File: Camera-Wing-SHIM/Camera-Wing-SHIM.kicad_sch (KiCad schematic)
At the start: 3 parts, among them J1 Pico RHS Headers, J2 Conn_01x06_Pin, J3 Conn_01x06_Socket

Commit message: Made PCB
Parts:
- J1: footprint (none) -> Footprints-General:Pico-Wing-Shim-SPI
- J2: value Conn_01x06_Pin -> Pin Connection
- J3: value Conn_01x06_Socket -> JST Connection; footprint Connector_JST:JST_XH_B7B-XH-A_1x07_P2.50mm_Vertical -> Connector_JST:JST_XH_B6B-XH-A_1x06_P2.50mm_Vertical
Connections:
- net +3V3: now also J2.1 (Pin_1), J3.1 (Pin_1)
- net CLK: now also J2.3 (Pin_3), J3.3 (Pin_3)
- net CS: now also J2.6 (Pin_6), J3.6 (Pin_6)
- net GND: now also J2.2 (Pin_2), J3.2 (Pin_2)
- net MISO: now also J2.4 (Pin_4), J3.4 (Pin_4)
- net MOSI: now also J2.5 (Pin_5), J3.5 (Pin_5)
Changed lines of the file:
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@@
+    (stroke (width 0) (type default))
+  )
+  (wire (pts (xy 133.35 78.74) (xy 139.7 78.74))
+    (stroke (width 0) (type default))
+  )
+  (wire (pts (xy 191.77 71.12) (xy 191.77 73.66))
     (stroke (width 0) (type default))
   )
@@
     (stroke (width 0) (type default))
   )
+  (wire (pts (xy 133.35 73.66) (xy 139.7 73.66))
+    (stroke (width 0) (type default))
+  )
+  (wire (pts (xy 147.32 68.58) (xy 147.32 66.04))
+    (stroke (width 0) (type default))
+  )
+  (wire (pts (xy 133.35 71.12) (xy 147.32 71.12))
+    (stroke (width 0) (type default))
+  )
   (wire (pts (xy 80.01 59.69) (xy 80.01 62.23))
     (stroke (width 0) (type default))
@@
     (stroke (width 0) (type default))
   )
+  (wire (pts (xy 177.8 78.74) (xy 184.15 78.74))
+    (stroke (width 0) (type default))
+  )
+  (wire (pts (xy 177.8 81.28) (xy 184.15 81.28))
+    (stroke (width 0) (type default))
+  )
+  (wire (pts (xy 191.77 68.58) (xy 191.77 66.04))
+    (stroke (width 0) (type default))
+  )
   (wire (pts (xy 71.12 90.17) (xy 82.55 90.17))
     (stroke (width 0) (type default))
@@
     (stroke (width 0) (type default))
   )
+  (wire (pts (xy 147.32 71.12) (xy 147.32 73.66))
+    (stroke (width 0) (type default))
+  )
+  (wire (pts (xy 133.35 76.2) (xy 139.7 76.2))
+    (stroke (width 0) (type default))
+  )
+  (wire (pts (xy 177.8 76.2) (xy 184.15 76.2))
+    (stroke (width 0) (type default))
+  )
   (wire (pts (xy 71.12 97.79) (xy 82.55 97.79))
     (stroke (width 0) (type default))
@@
     (stroke (width 0) (type default))
   )
+  (wire (pts (xy 177.8 73.66) (xy 184.15 73.66))
+    (stroke (width 0) (type default))
+  )
+  (wire (pts (xy 177.8 68.58) (xy 191.77 68.58))
+    (stroke (width 0) (type default))
+  )
+  (wire (pts (xy 133.35 81.28) (xy 139.7 81.28))
+    (stroke (width 0) (type default))
+  )
+  (wire (pts (xy 177.8 71.12) (xy 191.77 71.12))
+    (stroke (width 0) (type default))
+  )
+  (wire (pts (xy 133.35 68.58) (xy 147.32 68.58))
+    (stroke (width 0) (type default))
+  )
+  (label "MOSI" (at 184.15 78.74 180) (fields_autoplaced)
+    (effects (font (size 1.27 1.27)) (justify right bottom))
+  )
+  (label "CLK" (at 139.7 73.66 180) (fields_autoplaced)
+    (effects (font (size 1.27 1.27)) (justify right bottom))
+  )
+  (label "CS" (at 184.15 81.28 180) (fields_autoplaced)
+    (effects (font (size 1.27 1.27)) (justify right bottom))
+  )
   (label "MISO" (at 82.55 97.79 180) (fields_autoplaced)
     (effects (font (size 1.27 1.27)) (justify right bottom))
   )
+  (label "MISO" (at 184.15 76.2 180) (fields_autoplaced)
+    (effects (font (size 1.27 1.27)) (justify right bottom))
+  )
   (label "CS" (at 82.55 95.25 180) (fields_autoplaced)
     (effects (font (size 1.27 1.27)) (justify right bottom))
   )
+  (label "MOSI" (at 139.7 78.74 180) (fields_autoplaced)
+    (effects (font (size 1.27 1.27)) (justify right bottom))
+  )
   (label "MOSI" (at 82.55 87.63 180) (fields_autoplaced)
     (effects (font (size 1.27 1.27)) (justify right bottom))
   )
   (label "CLK" (at 82.55 90.17 180) (fields_autoplaced)
+    (effects (font (size 1.27 1.27)) (justify right bottom))
+  )
+  (label "CLK" (at 184.15 73.66 180) (fields_autoplaced)
+    (effects (font (size 1.27 1.27)) (justify right bottom))
+  )
+  (label "CS" (at 139.7 81.28 180) (fields_autoplaced)
+    (effects (font (size 1.27 1.27)) (justify right bottom))
+  )
+  (label "MISO" (at 139.7 76.2 180) (fields_autoplaced)
     (effects (font (size 1.27 1.27)) (justify right bottom))
   )
@@
       (effects (font (size 1.27 1.27)))
     )
-    (property "Footprint" "" (at 66.04 72.39 0)
+    (property "Footprint" "Footprints-General:Pico-Wing-Shim-SPI" (at 66.04 72.39 0)
       (effects (font (size 1.27 1.27)) hide)
     )
@@
     )
   )
+  (symbol (lib_id "power:GND") (at 147.32 73.66 0) (unit 1)
+    (in_bom yes) (on_board yes) (dnp no) (fields_autoplaced)
+    (property "Reference" "#PWR05" (at 147.32 80.01 0)
+      (effects (font (size 1.27 1.27)) hide)
+    )
+    (property "Value" "GND" (at 147.32 78.74 0)
+      (effects (font (size 1.27 1.27)))
+    )
+    (property "Footprint" "" (at 147.32 73.66 0)
+      (effects (font (size 1.27 1.27)) hide)
+    )
+    (property "Datasheet" "" (at 147.32 73.66 0)
+      (effects (font (size 1.27 1.27)) hide)
+    )
+    (pin "1")
+    (instances
+      (project "Camera-Wing-SHIM"
+        (path "/573a4d9c-bd0f-4c16-a1f5-7ab3d68c8cde"
+          (reference "#PWR05") (unit 1)
+        )
+      )
+    )
+  )
   (symbol (lib_id "Connector:Conn_01x06_Pin") (at 128.27 73.66 0) (unit 1)
     (in_bom yes) (on_board yes) (dnp no) (fields_autoplaced)
@@
       (effects (font (size 1.27 1.27)))
     )
-    (property "Value" "Conn_01x06_Pin" (at 128.905 66.04 0)
+    (property "Value" "Pin Connection" (at 128.905 66.04 0)
       (effects (font (size 1.27 1.27)))
     )
@@
     )
   )
+  (symbol (lib_id "power:+3V3") (at 147.32 66.04 0) (unit 1)
+    (in_bom yes) (on_board yes) (dnp no) (fields_autoplaced)
+    (property "Reference" "#PWR04" (at 147.32 69.85 0)
+      (effects (font (size 1.27 1.27)) hide)
+    )
+    (property "Value" "+3V3" (at 147.32 60.96 0)
+      (effects (font (size 1.27 1.27)))
+    )
+    (property "Footprint" "" (at 147.32 66.04 0)
+      (effects (font (size 1.27 1.27)) hide)
+    )
+    (property "Datasheet" "" (at 147.32 66.04 0)
+      (effects (font (size 1.27 1.27)) hide)
+    )
+    (pin "1")
+    (instances
+      (project "Camera-Wing-SHIM"
+        (path "/573a4d9c-bd0f-4c16-a1f5-7ab3d68c8cde"
+          (reference "#PWR04") (unit 1)
+        )
+      )
+    )
+  )
   (symbol (lib_id "power:GND") (at 92.71 95.25 0) (unit 1)
     (in_bom yes) (on_board yes) (dnp no) (fields_autoplaced)
@@
       (effects (font (size 1.27 1.27)))
     )
-    (property "Value" "Conn_01x06_Socket" (at 173.355 66.04 0)
-      (effects (font (size 1.27 1.27)))
-    )
-    (property "Footprint" "Connector_JST:JST_XH_B7B-XH-A_1x07_P2.50mm_Vertical" (at 172.72 73.66 0)
+    (property "Value" "JST Connection" (at 173.355 66.04 0)
+      (effects (font (size 1.27 1.27)))
+    )
+    (property "Footprint" "Connector_JST:JST_XH_B6B-XH-A_1x06_P2.50mm_Vertical" (at 172.72 73.66 0)
       (effects (font (size 1.27 1.27)) hide)
     )
@@
     )
   )
+  (symbol (lib_id "power:GND") (at 191.77 73.66 0) (unit 1)
+    (in_bom yes) (on_board yes) (dnp no) (fields_autoplaced)
+    (property "Reference" "#PWR07" (at 191.77 80.01 0)
+      (effects (font (size 1.27 1.27)) hide)
+    )
+    (property "Value" "GND" (at 191.77 78.74 0)
+      (effects (font (size 1.27 1.27)))
+    )
+    (property "Footprint" "" (at 191.77 73.66 0)
+      (effects (font (size 1.27 1.27)) hide)
+    )
+    (property "Datasheet" "" (at 191.77 73.66 0)
+      (effects (font (size 1.27 1.27)) hide)
+    )
+    (pin "1")
+    (instances
+      (project "Camera-Wing-SHIM"
+        (path "/573a4d9c-bd0f-4c16-a1f5-7ab3d68c8cde"
+          (reference "#PWR07") (unit 1)
+        )
+      )
+    )
+  )
   (symbol (lib_id "power:+3V3") (at 80.01 52.07 0) (unit 1)
     (in_bom yes) (on_board yes) (dnp no) (fields_autoplaced)
@@
         )
       )
+    )
+  )
+  (symbol (lib_id "power:+3V3") (at 191.77 66.04 0) (unit 1)
+    (in_bom yes) (on_board yes) (dnp no) (fields_autoplaced)
+    (property "Reference" "#PWR06" (at 191.77 69.85 0)
+      (effects (font (size 1.27 1.27)) hide)
+    )
+    (property "Value" "+3V3" (at 191.77 60.96 0)
+      (effects (font (size 1.27 1.27)))
+    )
+    (property "Footprint" "" (at 191.77 66.04 0)
+      (effects (font (size 1.27 1.27)) hide)
+    )
+    (property "Datasheet" "" (at 191.77 66.04 0)
+      (effects (font (size 1.27 1.27)) hide)
+    )
+    (pin "1")
+    (instances
+      (project "Camera-Wing-SHIM"
+        (path "/573a4d9c-bd0f-4c16-a1f5-7ab3d68c8cde"
+          (reference "#PWR06") (unit 1)
+        )
+      )

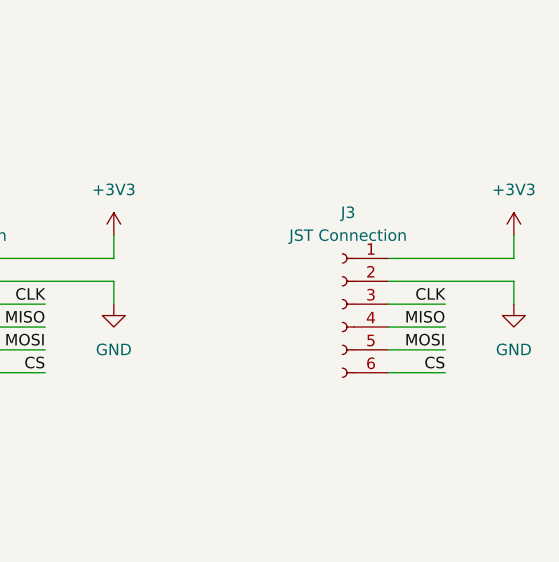
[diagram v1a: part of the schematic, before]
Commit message: Moved to SMD header
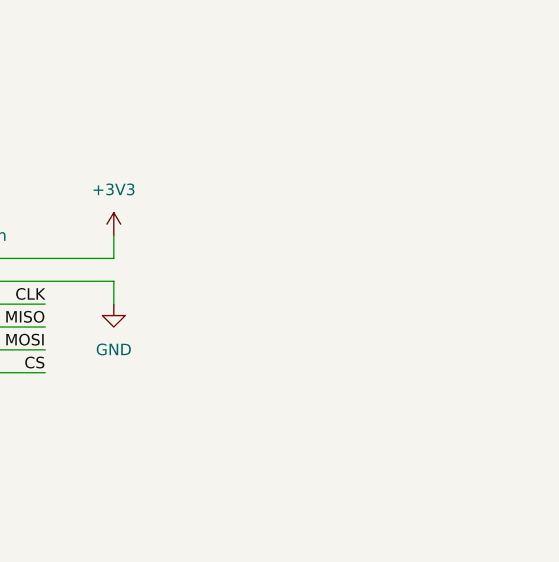
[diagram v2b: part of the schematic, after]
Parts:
- removed J3: JST Connection, Connector_JST:JST_XH_B6B-XH-A_1x06_P2.50mm_Vertical, symbol Connector:Conn_01x06_Socket
- J2: footprint Connector_PinHeader_2.54mm:PinHeader_1x06_P2.54mm_Vertical -> Liam-Footprints:6-pin-SMD-R2
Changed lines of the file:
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@@
-    (stroke (width 0) (type default))
-  )
-  (wire (pts (xy 191.77 71.12) (xy 191.77 73.66))
     (stroke (width 0) (type default))
   )
@@
     (stroke (width 0) (type default))
   )
-  (wire (pts (xy 177.8 78.74) (xy 184.15 78.74))
-    (stroke (width 0) (type default))
-  )
-  (wire (pts (xy 177.8 81.28) (xy 184.15 81.28))
-    (stroke (width 0) (type default))
-  )
-  (wire (pts (xy 191.77 68.58) (xy 191.77 66.04))
-    (stroke (width 0) (type default))
-  )
   (wire (pts (xy 71.12 90.17) (xy 82.55 90.17))
     (stroke (width 0) (type default))
@@
     (stroke (width 0) (type default))
   )
-  (wire (pts (xy 177.8 76.2) (xy 184.15 76.2))
-    (stroke (width 0) (type default))
-  )
   (wire (pts (xy 71.12 97.79) (xy 82.55 97.79))
     (stroke (width 0) (type default))
@@
     (stroke (width 0) (type default))
   )
-  (wire (pts (xy 177.8 73.66) (xy 184.15 73.66))
-    (stroke (width 0) (type default))
-  )
-  (wire (pts (xy 177.8 68.58) (xy 191.77 68.58))
-    (stroke (width 0) (type default))
-  )
   (wire (pts (xy 133.35 81.28) (xy 139.7 81.28))
     (stroke (width 0) (type default))
   )
-  (wire (pts (xy 177.8 71.12) (xy 191.77 71.12))
-    (stroke (width 0) (type default))
-  )
   (wire (pts (xy 133.35 68.58) (xy 147.32 68.58))
     (stroke (width 0) (type default))
   )
-  (label "MOSI" (at 184.15 78.74 180) (fields_autoplaced)
-    (effects (font (size 1.27 1.27)) (justify right bottom))
-  )
   (label "CLK" (at 139.7 73.66 180) (fields_autoplaced)
     (effects (font (size 1.27 1.27)) (justify right bottom))
   )
-  (label "CS" (at 184.15 81.28 180) (fields_autoplaced)
-    (effects (font (size 1.27 1.27)) (justify right bottom))
-  )
   (label "MISO" (at 82.55 97.79 180) (fields_autoplaced)
     (effects (font (size 1.27 1.27)) (justify right bottom))
   )
-  (label "MISO" (at 184.15 76.2 180) (fields_autoplaced)
-    (effects (font (size 1.27 1.27)) (justify right bottom))
-  )
   (label "CS" (at 82.55 95.25 180) (fields_autoplaced)
     (effects (font (size 1.27 1.27)) (justify right bottom))
@@
   )
   (label "CLK" (at 82.55 90.17 180) (fields_autoplaced)
-    (effects (font (size 1.27 1.27)) (justify right bottom))
-  )
-  (label "CLK" (at 184.15 73.66 180) (fields_autoplaced)
     (effects (font (size 1.27 1.27)) (justify right bottom))
   )
@@
       (effects (font (size 1.27 1.27)))
     )
-    (property "Footprint" "Connector_PinHeader_2.54mm:PinHeader_1x06_P2.54mm_Vertical" (at 128.27 73.66 0)
+    (property "Footprint" "Liam-Footprints:6-pin-SMD-R2" (at 128.27 73.66 0)
       (effects (font (size 1.27 1.27)) hide)
     )
@@
     )
   )
-  (symbol (lib_id "Connector:Conn_01x06_Socket") (at 172.72 73.66 0) (mirror y) (unit 1)
-    (in_bom yes) (on_board yes) (dnp no) (fields_autoplaced)
-    (property "Reference" "J3" (at 173.355 63.5 0)
-      (effects (font (size 1.27 1.27)))
-    )
-    (property "Value" "JST Connection" (at 173.355 66.04 0)
-      (effects (font (size 1.27 1.27)))
-    )
-    (property "Footprint" "Connector_JST:JST_XH_B6B-XH-A_1x06_P2.50mm_Vertical" (at 172.72 73.66 0)
-      (effects (font (size 1.27 1.27)) hide)
-    )
-    (property "Datasheet" "~" (at 172.72 73.66 0)
-      (effects (font (size 1.27 1.27)) hide)
-    )
-    (pin "4")
-    (pin "6")
-    (pin "5")
-    (pin "1")
-    (pin "3")
-    (pin "2")
-    (instances
-      (project "Camera-Wing-SHIM"
-        (path "/573a4d9c-bd0f-4c16-a1f5-7ab3d68c8cde"
-          (reference "J3") (unit 1)
-        )
-      )
-    )
-  )
-  (symbol (lib_id "power:GND") (at 191.77 73.66 0) (unit 1)
-    (in_bom yes) (on_board yes) (dnp no) (fields_autoplaced)
-    (property "Reference" "#PWR07" (at 191.77 80.01 0)
-      (effects (font (size 1.27 1.27)) hide)
-    )
-    (property "Value" "GND" (at 191.77 78.74 0)
-      (effects (font (size 1.27 1.27)))
-    )
-    (property "Footprint" "" (at 191.77 73.66 0)
-      (effects (font (size 1.27 1.27)) hide)
-    )
-    (property "Datasheet" "" (at 191.77 73.66 0)
-      (effects (font (size 1.27 1.27)) hide)
-    )
-    (pin "1")
-    (instances
-      (project "Camera-Wing-SHIM"
-        (path "/573a4d9c-bd0f-4c16-a1f5-7ab3d68c8cde"
-          (reference "#PWR07") (unit 1)
-        )
-      )
-    )
-  )
   (symbol (lib_id "power:+3V3") (at 80.01 52.07 0) (unit 1)
     (in_bom yes) (on_board yes) (dnp no) (fields_autoplaced)
@@
         )
       )
-    )
-  )
-  (symbol (lib_id "power:+3V3") (at 191.77 66.04 0) (unit 1)
-    (in_bom yes) (on_board yes) (dnp no) (fields_autoplaced)
-    (property "Reference" "#PWR06" (at 191.77 69.85 0)
-      (effects (font (size 1.27 1.27)) hide)
-    )
-    (property "Value" "+3V3" (at 191.77 60.96 0)
-      (effects (font (size 1.27 1.27)))
-    )
-    (property "Footprint" "" (at 191.77 66.04 0)
-      (effects (font (size 1.27 1.27)) hide)
-    )
-    (property "Datasheet" "" (at 191.77 66.04 0)
-      (effects (font (size 1.27 1.27)) hide)
-    )
-    (pin "1")
-    (instances
-      (project "Camera-Wing-SHIM"
-        (path "/573a4d9c-bd0f-4c16-a1f5-7ab3d68c8cde"
-          (reference "#PWR06") (unit 1)
-        )
-      )
